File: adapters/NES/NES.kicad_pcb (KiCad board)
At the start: 2 copper layers, 58.4 x 38.1 mm, 20 parts, among them J1 Port 1, J2 Port 2, J3 NES_Gamepad, M1 Mounting, M2 Mounting, M3 Mounting, M4 Mounting, SW1 START, U1 CD4021

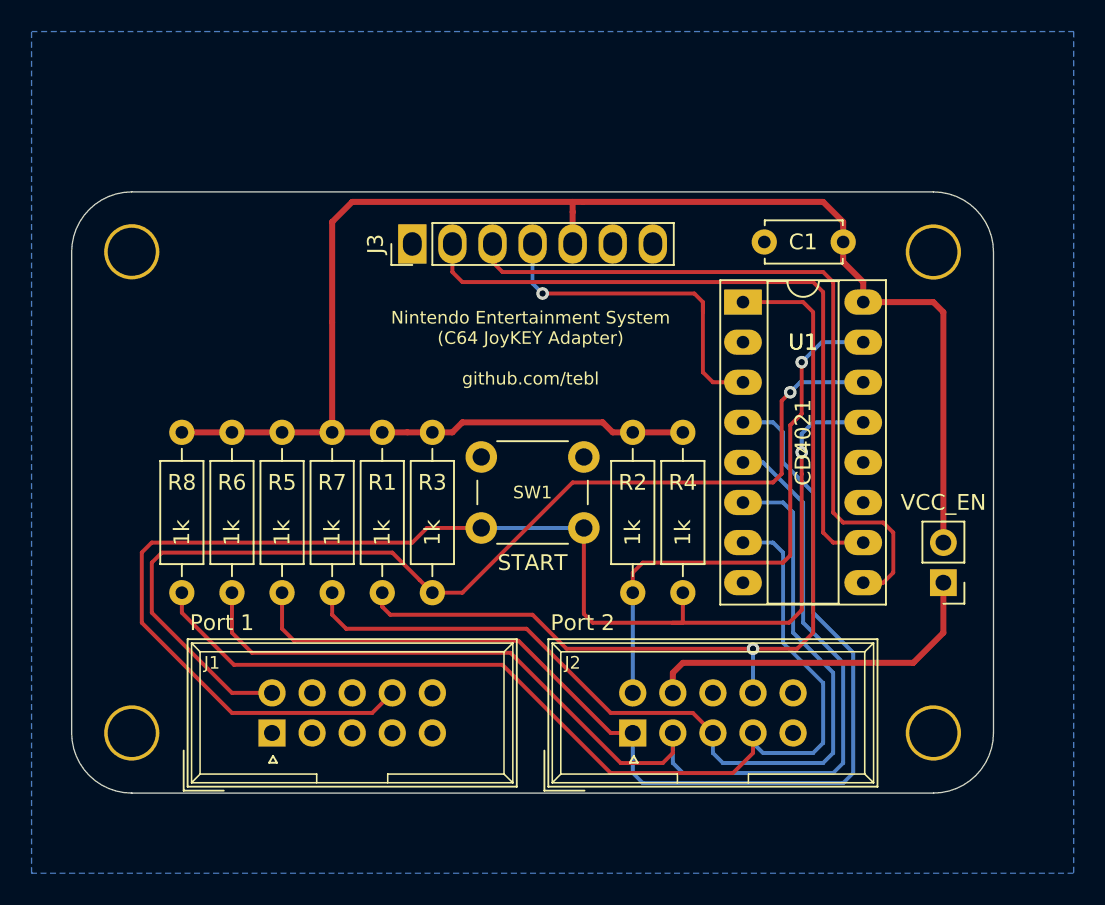
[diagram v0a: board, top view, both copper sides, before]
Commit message: Add strain relief
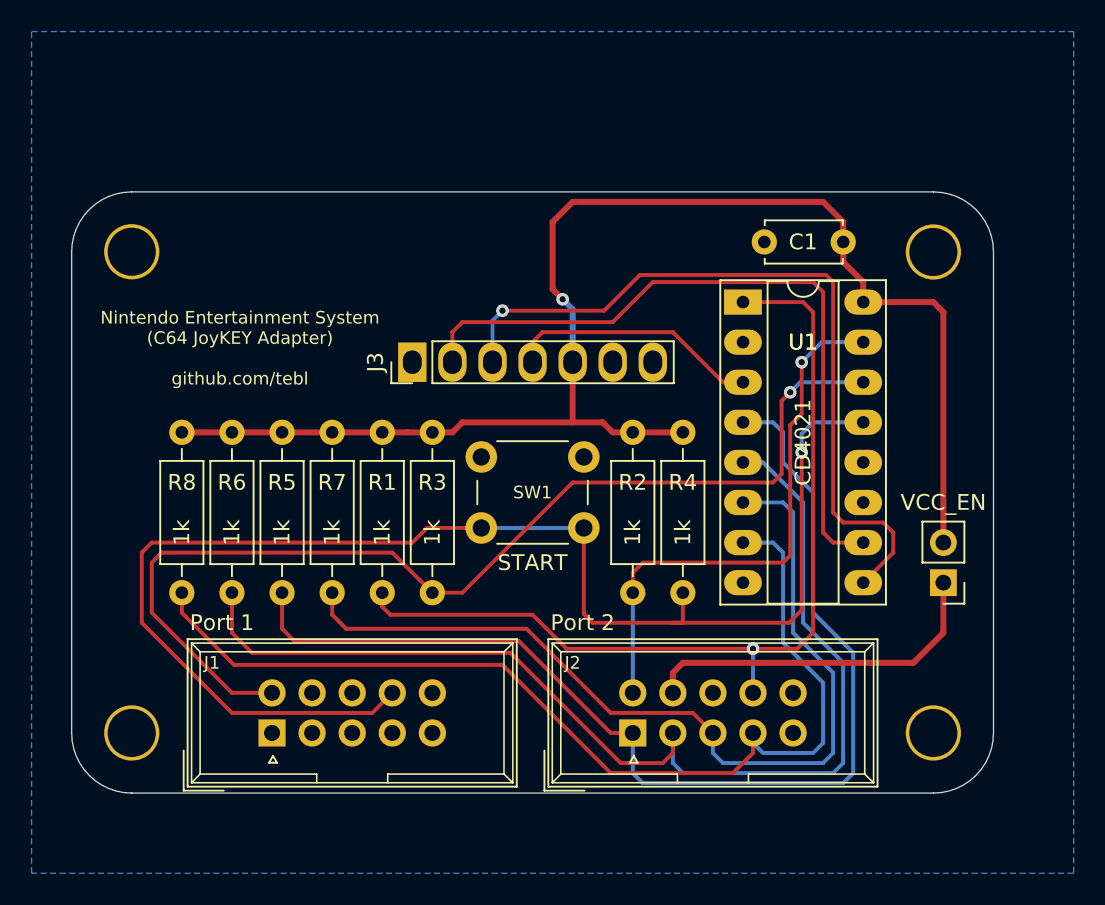
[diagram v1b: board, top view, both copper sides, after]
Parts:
- moved G*** 18.4 mm to (125.6, 83.1)
- moved J3 7.49 mm to (136.5, 84.5)
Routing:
- net VCC: track 107.3 -> 90.5 mm, vias 0 -> 1
- net DATA: track 21.7 -> 16.2 mm, vias 1 -> 0
- net LATCH: track 46.9 -> 48.5 mm, vias 0 -> 1
- net CLK: track 43.8 -> 45.0 mm
